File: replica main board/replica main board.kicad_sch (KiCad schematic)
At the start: 92 parts, among them J1 BNC in, J2 Charger in, Q1 2N5179, Q2 2N5484, Q3 2N5771, Q4 2N3906, Q5 2N5179, Q6 2N3906, U1 11C90, U2 10116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

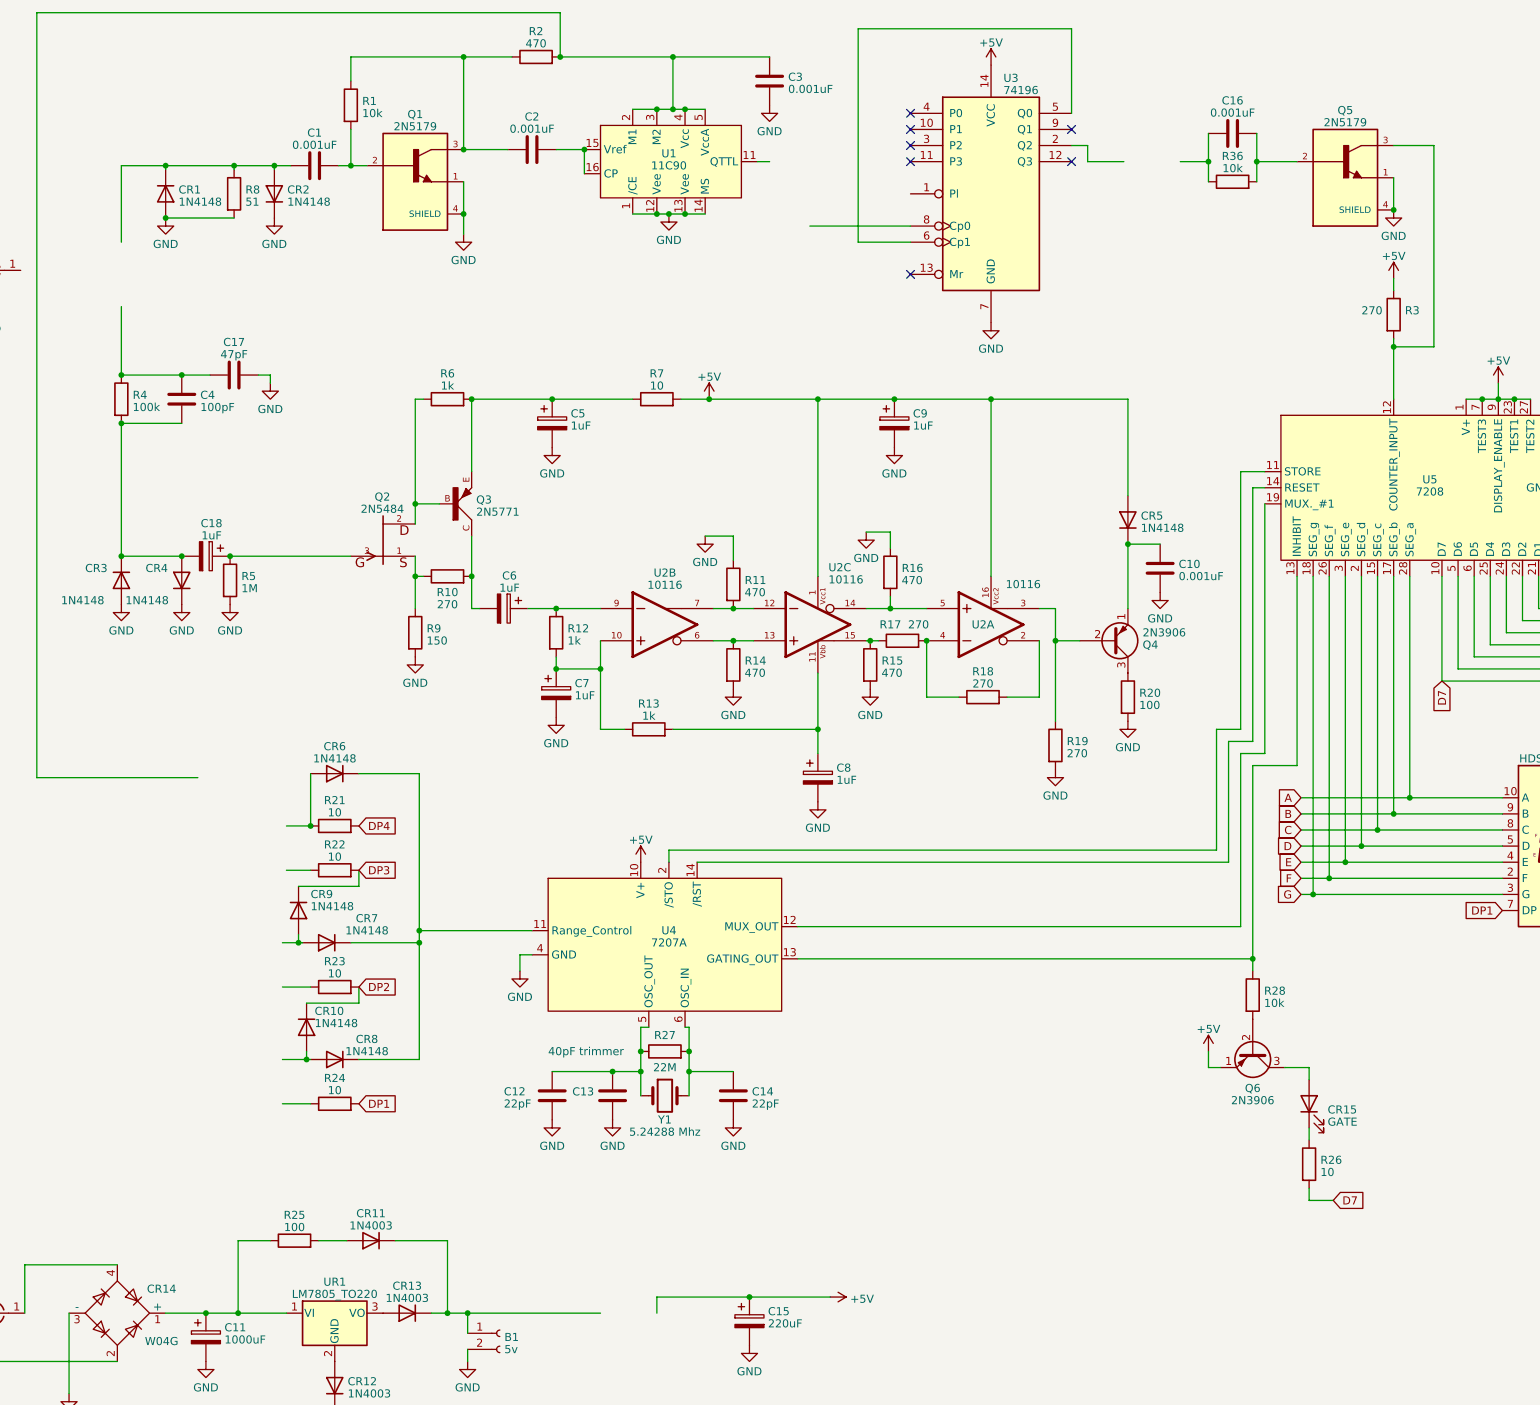
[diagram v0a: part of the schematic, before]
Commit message: board laid out per manual design plus inferences for top layer
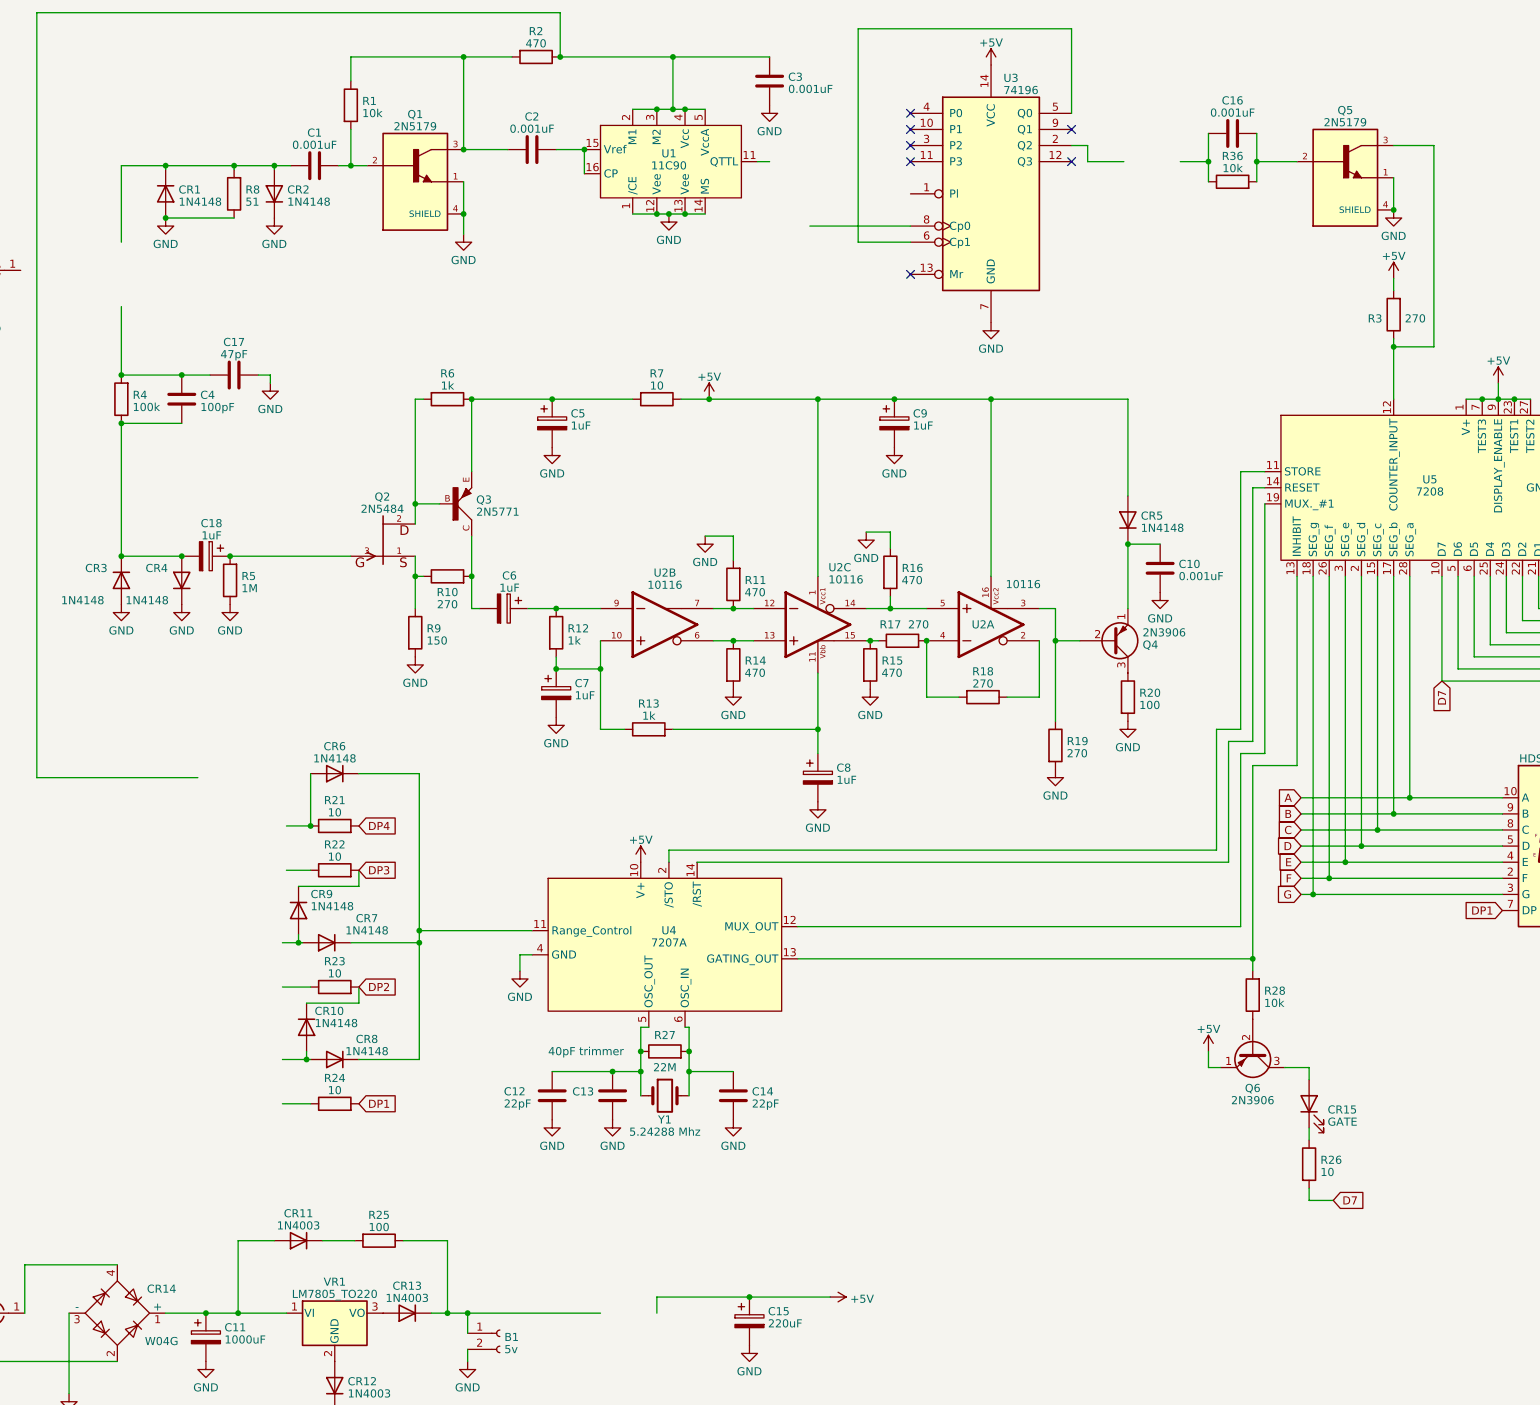
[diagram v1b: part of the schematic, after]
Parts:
- B1, J2: footprint (none) -> TerminalBlock:TerminalBlock_Wuerth_691311400102_P7.62mm
- C1, C10, C12, C14, C16, C17, C2, C3, C4: footprint (none) -> Capacitor_THT:C_Disc_D4.7mm_W2.5mm_P5.00mm
- C11: footprint (none) -> Capacitor_THT:CP_Radial_D10.0mm_P5.00mm
- C13: footprint (none) -> Capacitor_THT:C_Radial_D16.0mm_H25.0mm_P7.50mm
- C15: footprint (none) -> Capacitor_THT:CP_Radial_D8.0mm_P5.00mm
- C18, C5, C6, C7, C8, C9: footprint (none) -> Capacitor_THT:CP_Radial_Tantal_D4.5mm_P2.50mm
- CR1, CR10, CR3, CR4, CR5, CR6, CR7, CR8, CR9: footprint Diode_THT:D_DO-35_SOD27_P7.62mm_Horizontal -> Diode_THT:D_DO-41_SOD81_P2.54mm_Vertical_KathodeUp
- CR11, CR12: footprint Diode_THT:D_DO-41_SOD81_P10.16mm_Horizontal -> Diode_THT:D_DO-41_SOD81_P5.08mm_Vertical_AnodeUp
- CR13: footprint Diode_THT:D_DO-41_SOD81_P10.16mm_Horizontal -> Diode_THT:D_DO-41_SOD81_P5.08mm_Vertical_KathodeUp
- CR2: footprint Diode_THT:D_DO-35_SOD27_P7.62mm_Horizontal -> Diode_THT:D_DO-41_SOD81_P3.81mm_Vertical_AnodeUp
- Q1: footprint TO127P584H533-4N -> Evan's parts:TO127P584H533-4N
- Q2: footprint TRANS_2N5484 -> Package_TO_SOT_THT:TO-92_Wide
- Q3: footprint TO92D -> Package_TO_SOT_THT:TO-92_Wide
- Q4, Q6: footprint Package_TO_SOT_THT:TO-92_Inline -> Package_TO_SOT_THT:TO-92_Wide
- Q5: footprint TO127P584H533-4N -> Package_TO_SOT_THT:TO-92_Wide
- R1, R2, R28, R36, R4, R5, R8: footprint (none) -> Resistor_THT:R_Axial_DIN0207_L6.3mm_D2.5mm_P5.08mm_Vertical
- R11, R12, R13, R14, R15, R16, R17, R18, R19, R20, R25, R27, R3, R7: footprint (none) -> Resistor_THT:R_Axial_DIN0207_L6.3mm_D2.5mm_P2.54mm_Vertical
- U1, U2: footprint (none) -> Package_DIP:DIP-16_W7.62mm
- U3, U4: footprint (none) -> Package_DIP:DIP-14_W7.62mm
- U5: footprint (none) -> Package_DIP:DIP-28_W15.24mm
- VR1: renamed from UR1; footprint Package_TO_SOT_THT:TO-220-3_Vertical -> Package_TO_SOT_THT:TO-220-3_Horizontal_TabDown
- Y1: footprint (none) -> Crystal:Crystal_HC18-U_Vertical
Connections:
- net +5V: now also R3.2, R7.1; no longer R3.1, R7.2
- net GND: now also C17.1, R11.2, R5.1, R8.1; no longer C17.2, R11.1, R5.2, R8.2
- net at Q2.2, Q3.B: now also R6.2; no longer R6.1
- net at C18.1, Q2.3: now also R5.2; no longer R5.1
- net at Q5.3, U5.12 (COUNTER_INPUT): now also R3.1; no longer R3.2
- net at C2.1, Q1.3, R1.1: now also R2.2; no longer R2.1
- net at C3.1, U1.2 (M1), U1.3 (M2)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: now also R2.1; no longer R2.2
- net at C18.2, C4.2, CR3.1 (K)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: now also R4.1; no longer R4.2
- net at C11.1, CR14.1 (+), VR1.1 (VI): now also CR11.2 (A); no longer R25.1
- net at B1.1 (Pin_1), CR13.1 (K): now also R25.1; no longer CR11.1 (K)
- net at U2.12, U2.7: now also R11.1; no longer R11.2
- net at C1.1, CR1.1 (K), CR2.2 (A): now also R8.2; no longer R8.1
- net at R25.2: now also CR11.1 (K); no longer CR11.2 (A)
- net at R17.2, U2.4: now also R18.2; no longer R18.1
- net at U2.2: now also R18.1; no longer R18.2
- net at U4.13 (GATING_OUT), U5.13 (INHIBIT): now also R28.2; no longer R28.1
- net at Q6.2 (B): now also R28.1; no longer R28.2
- net at C5.1, Q3.E: now also R6.1, R7.2; no longer R6.2, R7.1
- new net: C17.2, C4.1, R4.2
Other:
- moved on the sheet: C17, CR11, R11, R18, R2, R25, R28, R3, R4, R5, R6, R7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

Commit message: finished layout
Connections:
- net at U4.14 (/RST), U5.14 (RESET): now also U4.9 (NC)
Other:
- moved on the sheet: C1, C10, C12, C13, C14, C16, C17, C18, C2, C3, C4, C5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
